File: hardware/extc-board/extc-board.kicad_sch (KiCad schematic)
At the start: 18 parts, among them J1 GH link to INT, J2 bus pads, J3 PTSM 0,5/2-HH-SMD 24VAC input, J4 PTSM 0,5/2-HV-SMD 5VDC output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, U1 DS2482-100 (0x18), U3 TMR 12-4811WI

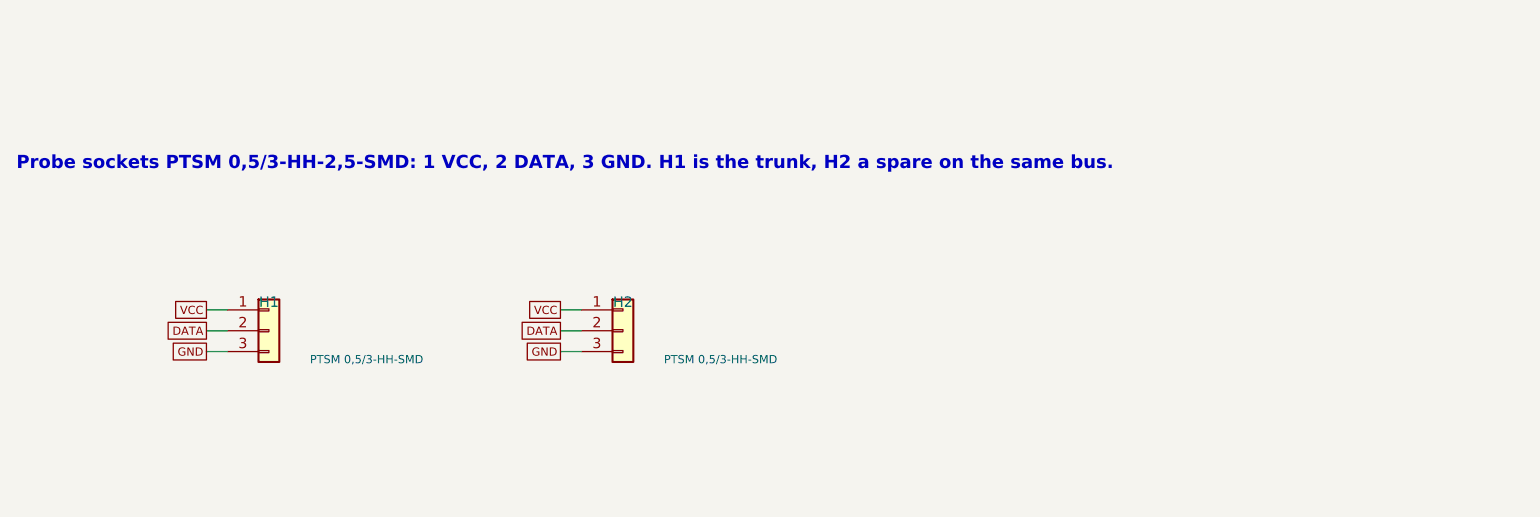
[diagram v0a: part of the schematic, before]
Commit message: Rev C: fit check against Phoenix's STEP models; anchor pads moved 0.4 mm (#219)
* Rev C: fit check against Phoenix's STEP models; anchor pads moved 0.4 mm

hardware/fit-check.py lays the STEP models on the footprints of the
generated board and reports the margin of every solder foot inside its
pad and the play of every peg in its hole. It replaces the check in
KiCad's 3D viewer, and stands in for laying a header on a print until
the headers arrive.

Its first run found the horizontal header's anchor feet 0.1 mm off the
rear of their pads. The pads were placed 0.8 to 6.4 mm from the face; the
feet lie 1.5 to 6.5 mm from it. Phoenix's drawing puts the pad's end
0.2 mm past the start of the signal pads, which I had read as 0.2 mm
short of it. The pads are now 1.2 to 6.8 mm from the face, centred on
the feet with 0.3 mm to spare at each end.

The three STEP models are in hardware/vendor with the housing models.

Co-Authored-By: Claude Fable 5.1 <noreply@anthropic.com>

* Rev C: fit check against the models of the parts being fitted; H1 and H2 are HH0

David supplied the models of the three connectors he is fitting. The
check now lays each on its own footprint: 1808200 on H1 and H2, 1778764
on J3, 1778696 on J4. Every foot lies on its pad and every peg in its
hole.

1808200 is the HH0 header, the HH without its two locating pegs; body,
anchors, leads and latch windows are the same. The footprint keeps its
peg holes, which stay empty under an HH0, so the board takes either.

The board's copper and gerbers are unchanged: only the value of H1 and
H2 in the board, schematic and BOM. DRC is still clean.

The housing check is closed: David confirms a plug seats with the header
faces on the board edge.

Co-Authored-By: Claude Fable 5.1 <noreply@anthropic.com>

---------

Co-authored-by: Claude Fable 5.1 <noreply@anthropic.com>
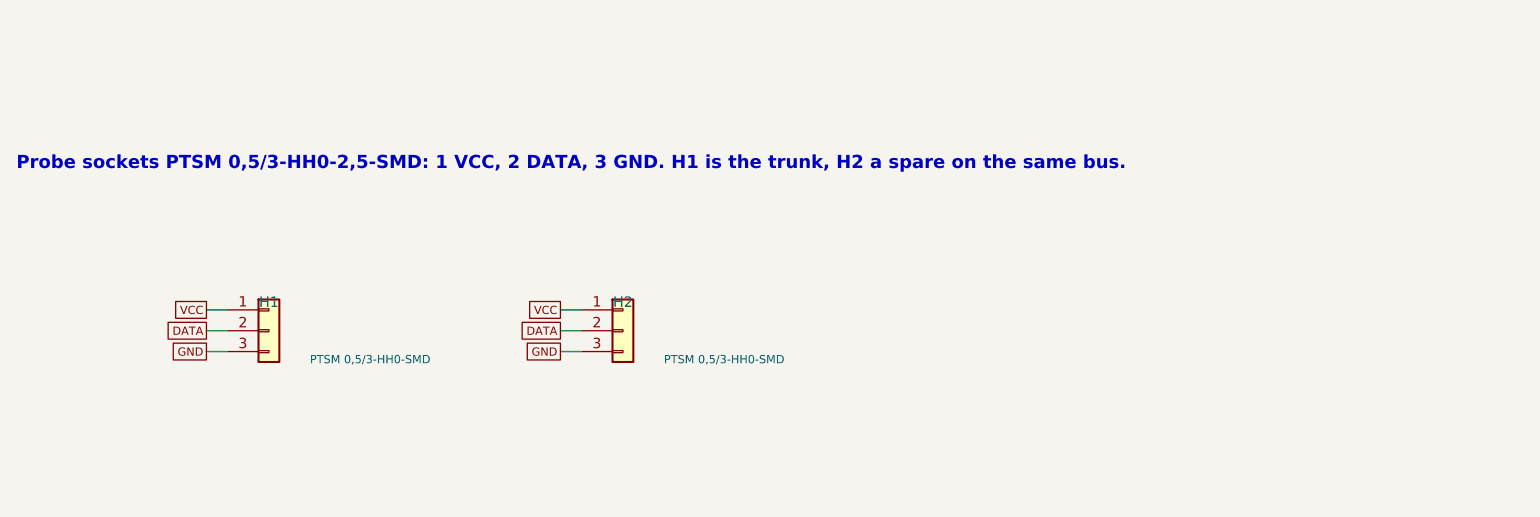
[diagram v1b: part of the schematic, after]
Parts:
- H1, H2: value PTSM 0,5/3-HH-SMD -> PTSM 0,5/3-HH0-SMD
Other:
- note added: "Probe sockets PTSM 0,5/3-HH0-2,5-SMD: 1 VCC, 2 DATA, 3 GND. H1 is the trunk, H2 a spare on the same bus."
- note removed: "Probe sockets PTSM 0,5/3-HH-2,5-SMD: 1 VCC, 2 DATA, 3 GND. H1 is the trunk, H2 a spare on the same bus."
